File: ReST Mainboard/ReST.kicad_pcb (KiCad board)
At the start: 2 copper layers, 100 x 100 mm, 104 parts, among them IC1 AT24C128, P1 CONN_02X08, P10 CONN_01X04, P11 CONN_01X04, P12 CONN_02X04, P13 CONN_01X03, P14 CONN_02X03, P15 CONN_01X05, P16 CONN_01X03, P17 CONN_01X04, P18 CONN_02X04, P19 CONN_01X04, P2 CONN_02X08, P20 CONN_02X04, P21 CONN_02X04, P22 CONN_01X03, P23 SCREW_01X03, P24 CONN_01X03, P25 SCREW_01X03, P26 CONN_01X03, P27 SCREW_01X03, P28 CONN_01X03, P29 SCREW_01X03, P3 CONN_02X07, P30 CONN_01X03, P31 SCREW_01X03, P32 CONN_01X03, P33 SCREW_01X03, P34 CONN_01X03, P35 SCREW_01X04, P36 SCREW_01X04, P37 SCREW_01X04, P38 SCREW_01X04, P39 CONN_02X04, P4 CONN_02X10, P40 CONN_01X04, P41 CONN_01X04, P42 CONN_01X04, P43 CONN_02X03, P44 CONN_02X03, P45 CONN_02X03, P46 CONN_02X03, P5 USB_OTG, P6 CONN_02X05, P7 CONN_02X05, P8 CONN_01X09, P9 CONN_01X02, SW1 SW-SPST-NO, U1 STM32F103VE, U2 USBLC6-2, U3 L7805ACD2T-TR, U4 LM2574N-ADJ, U5 POLOLU_A4988, U6 POLOLU_A4988, U7 POLOLU_A4988, U8 POLOLU_A4988, X1 Crystal_Small

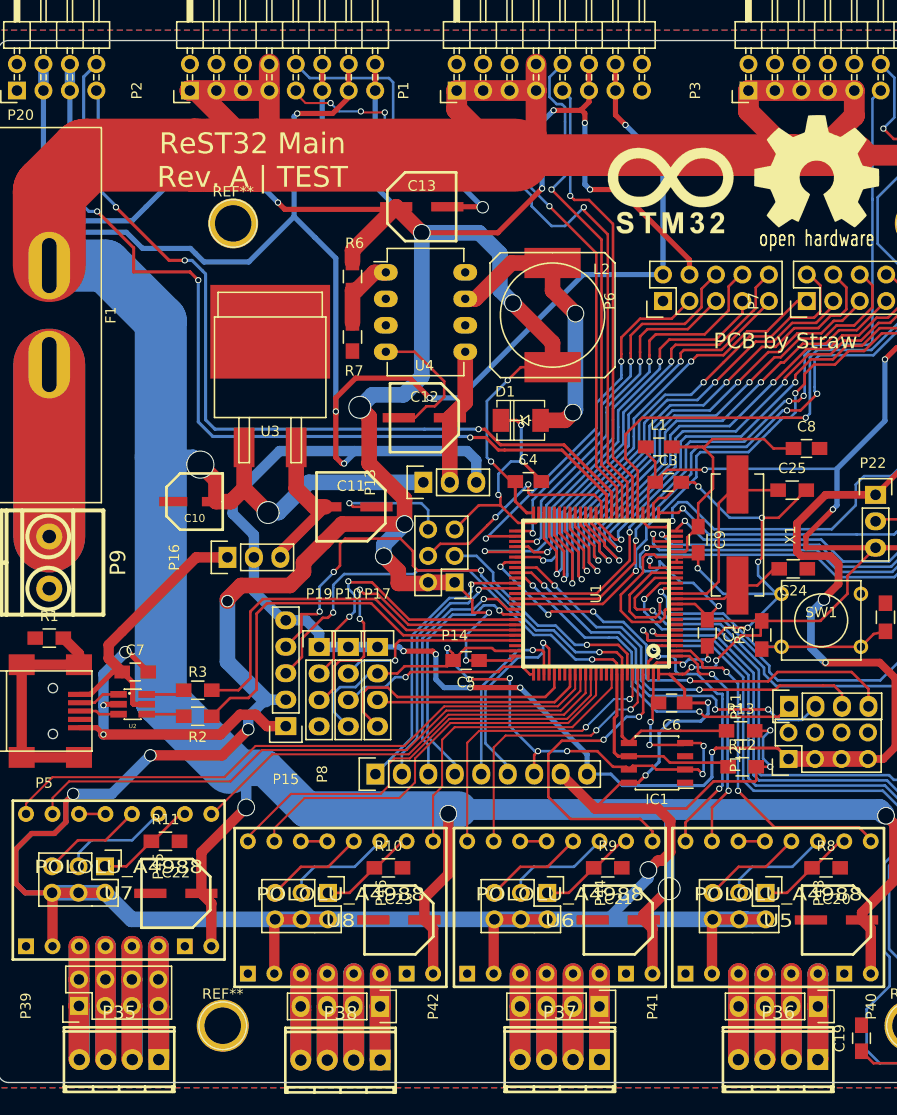
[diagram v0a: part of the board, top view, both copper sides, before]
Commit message: Finally removed all unnecessary Libs and added Heatsink for 5V Regulator
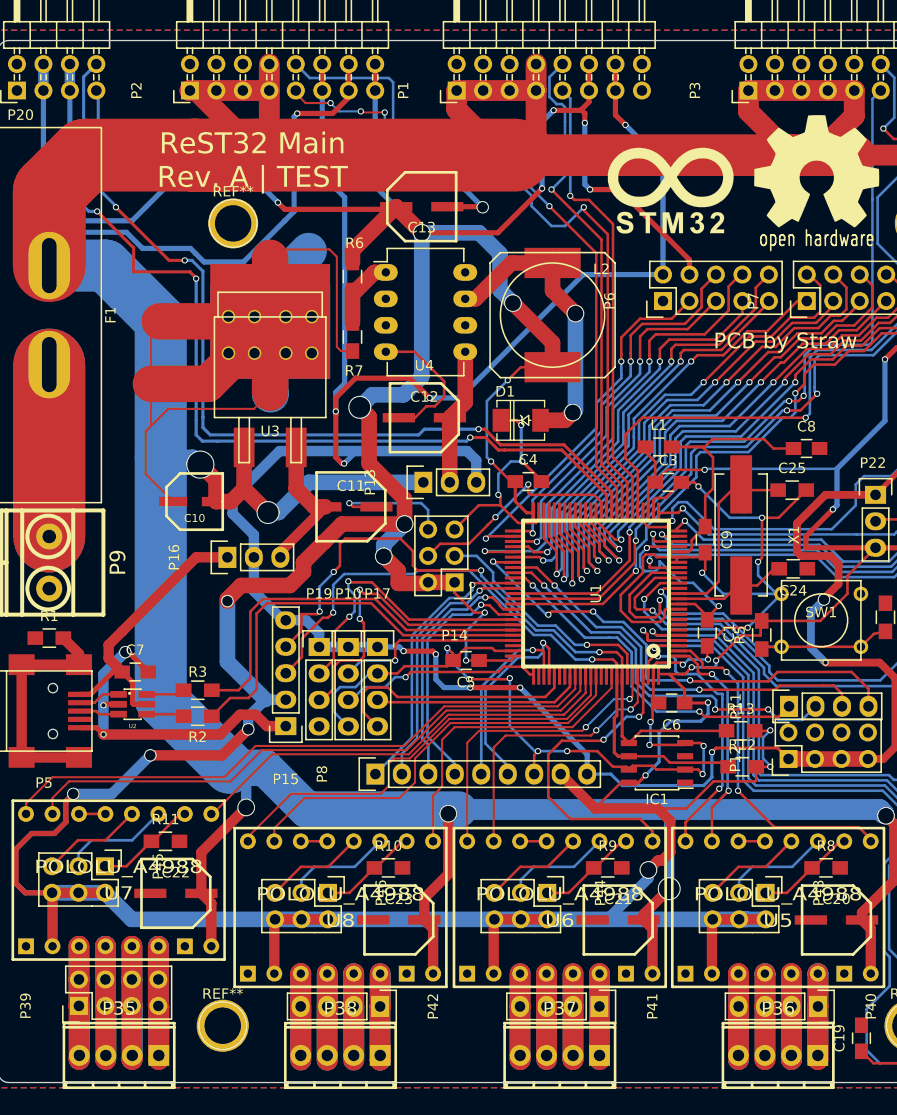
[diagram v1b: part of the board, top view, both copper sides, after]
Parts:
- C10: footprint ok-polcaps-panasonic:CP-PANASONIC-SMT_C -> ReST-Library:CP-PANASONIC-SMT_C
- C11, C12, C13: footprint ok-polcaps-panasonic:CP-PANASONIC-SMT_D -> ReST-Library:CP-PANASONIC-SMT_D
- C20, C21, C22, C23: footprint ok-polcaps-panasonic:CP-PANASONIC-SMT_D8 -> ReST-Library:CP-PANASONIC-SMT_D8
- U1: footprint ok-ic-smd:LQFP100-14x14 -> ReST-Library:LQFP100-14x14
- U3: footprint TO_SOT_Packages_SMD:SOT-404 -> ReST-Library:SOT-404
- moved C9 0.68 mm to (167.3, 103.3)
- moved P38 0.45 mm to (132.3, 152.8)
- moved P35 0.40 mm to (111.0, 152.8)
- moved P36 0.40 mm to (174.3, 152.8)
- moved P37 0.40 mm to (153.3, 152.8)
- moved X1 0.35 mm to (170.8, 102.9)
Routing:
- net GND: track 261.6 -> 364.0 mm
- net +5V: track 320.6 -> 327.7 mm
- net /SERVO1: track 46.4 -> 47.9 mm
- net /PWM-BED: track 86.8 -> 88.1 mm
- net /T0: track 81.0 -> 82.1 mm
- net Net-(C8-Pad1): track 24.2 -> 25.0 mm
- net /EXTRA2: track 24.1 -> 24.9 mm
- net +3V3: track 652.6 -> 652.0 mm

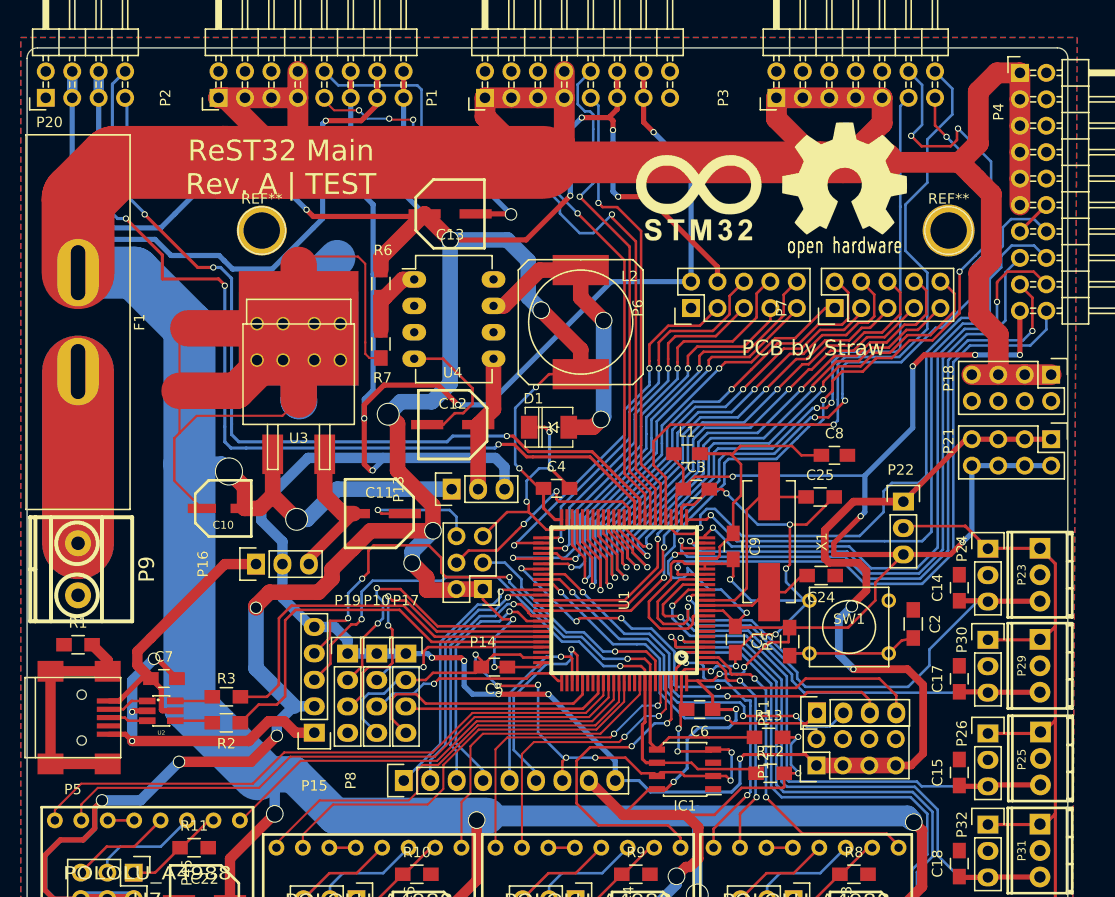
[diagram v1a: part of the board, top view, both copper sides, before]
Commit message: Added IRLML2502 Module and added Ground vias everywhere
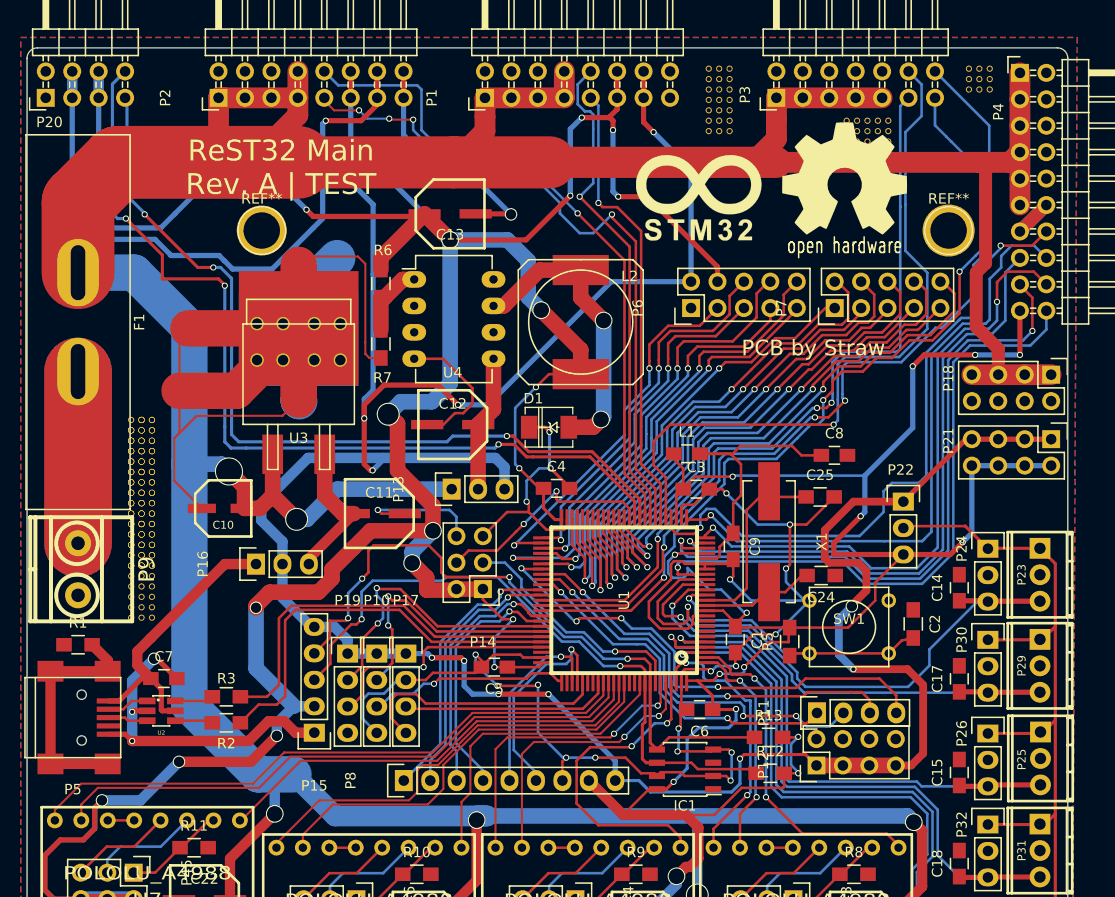
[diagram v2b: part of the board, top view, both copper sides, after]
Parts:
- added 1111: , ReST-Library:VIA-0.6mm, F.Cu at (189.9, 57.5)
- added 11111: , ReST-Library:VIA-0.6mm, F.Cu at (164.9, 57.5)
- added 111111: , ReST-Library:VIA-0.6mm, F.Cu at (178.2, 62.5)
- added 11111110, 111111110, 1111111110: , ReST-Library:VIA-0.6mm, F.Cu at (109.5, 100.2)
- added 11111111, 111111111, 1111111111: , ReST-Library:VIA-0.6mm, F.Cu at (109.5, 101.2)
- added 111111111: , ReST-Library:VIA-0.6mm, F.Cu at (109.5, 91.2)
- added 1111111112, 111111112, 11111112: , ReST-Library:VIA-0.6mm, F.Cu at (109.5, 102.2)
- added 1111111113, 111111113, 11111113: , ReST-Library:VIA-0.6mm, F.Cu at (109.5, 103.2)
- added 1111111114, 111111114, 11111114: , ReST-Library:VIA-0.6mm, F.Cu at (109.5, 104.2)
- added 1111111115, 111111115, 11111115: , ReST-Library:VIA-0.6mm, F.Cu at (109.5, 105.2)
- added 1111111116: , ReST-Library:VIA-0.6mm, F.Cu at (109.5, 106.2)
- added 1111111117: , ReST-Library:VIA-0.6mm, F.Cu at (109.5, 107.2)
- added 1111111118: , ReST-Library:VIA-0.6mm, F.Cu at (109.5, 108.2)
- added 1111111119: , ReST-Library:VIA-0.6mm, F.Cu at (109.5, 109.2)
- added 111111112, 11111112, 1111112: , ReST-Library:VIA-0.6mm, F.Cu at (109.5, 92.2)
- added 1111111120: , ReST-Library:VIA-0.6mm, F.Cu at (109.5, 110.2)
- added 111111113, 11111113, 1111113: , ReST-Library:VIA-0.6mm, F.Cu at (109.5, 93.2)
- added 111111114, 11111114, 1111114: , ReST-Library:VIA-0.6mm, F.Cu at (109.5, 94.2)
- added 111111115, 11111115, 1111115: , ReST-Library:VIA-0.6mm, F.Cu at (109.5, 95.2)
- added 111111116, 11111116, 1111116: , ReST-Library:VIA-0.6mm, F.Cu at (109.5, 96.2)
- added 111111117, 11111117, 1111117: , ReST-Library:VIA-0.6mm, F.Cu at (109.5, 97.2)
- added 111111118, 11111118, 1111118: , ReST-Library:VIA-0.6mm, F.Cu at (109.5, 98.2)
- added 111111119, 11111119, 1111119: , ReST-Library:VIA-0.6mm, F.Cu at (109.5, 99.2)
- added 111111121, 11111121, 1111121: , ReST-Library:VIA-0.6mm, F.Cu at (110.5, 91.2)
- added 1111111210, 111111210, 11111210: , ReST-Library:VIA-0.6mm, F.Cu at (110.5, 100.2)
- added 1111111211, 111111211, 11111211: , ReST-Library:VIA-0.6mm, F.Cu at (110.5, 101.2)
- added 1111111212, 111111212, 11111212: , ReST-Library:VIA-0.6mm, F.Cu at (110.5, 102.2)
- added 1111111213, 111111213, 11111213: , ReST-Library:VIA-0.6mm, F.Cu at (110.5, 103.2)
- added 1111111214, 111111214, 11111214: , ReST-Library:VIA-0.6mm, F.Cu at (110.5, 104.2)
- added 1111111215, 111111215, 11111215: , ReST-Library:VIA-0.6mm, F.Cu at (110.5, 105.2)
- added 1111111216: , ReST-Library:VIA-0.6mm, F.Cu at (110.5, 106.2)
- added 1111111217: , ReST-Library:VIA-0.6mm, F.Cu at (110.5, 107.2)
- added 1111111218: , ReST-Library:VIA-0.6mm, F.Cu at (110.5, 108.2)
- added 1111111219: , ReST-Library:VIA-0.6mm, F.Cu at (110.5, 109.2)
- added 111111122, 11111122, 1111122: , ReST-Library:VIA-0.6mm, F.Cu at (110.5, 92.2)
- added 1111111220: , ReST-Library:VIA-0.6mm, F.Cu at (110.5, 110.2)
- added 111111123, 11111123, 1111123: , ReST-Library:VIA-0.6mm, F.Cu at (110.5, 93.2)
- added 111111124, 11111124, 1111124: , ReST-Library:VIA-0.6mm, F.Cu at (110.5, 94.2)
- added 111111125, 11111125, 1111125: , ReST-Library:VIA-0.6mm, F.Cu at (110.5, 95.2)
- added 111111126, 11111126, 1111126: , ReST-Library:VIA-0.6mm, F.Cu at (110.5, 96.2)
- added 111111127, 11111127, 1111127: , ReST-Library:VIA-0.6mm, F.Cu at (110.5, 97.2)
- added 111111128, 11111128, 1111128: , ReST-Library:VIA-0.6mm, F.Cu at (110.5, 98.2)
- added 111111129, 11111129, 1111129: , ReST-Library:VIA-0.6mm, F.Cu at (110.5, 99.2)
- added 111111131, 11111131: , ReST-Library:VIA-0.6mm, F.Cu at (111.5, 91.2)
- added 1111111310, 111111310: , ReST-Library:VIA-0.6mm, F.Cu at (111.5, 100.2)
- added 1111111311, 111111311: , ReST-Library:VIA-0.6mm, F.Cu at (111.5, 101.2)
- added 1111111312, 111111312: , ReST-Library:VIA-0.6mm, F.Cu at (111.5, 102.2)
- added 1111111313, 111111313: , ReST-Library:VIA-0.6mm, F.Cu at (111.5, 103.2)
- added 1111111314, 111111314: , ReST-Library:VIA-0.6mm, F.Cu at (111.5, 104.2)
- added 1111111315, 111111315: , ReST-Library:VIA-0.6mm, F.Cu at (111.5, 105.2)
- added 1111111316: , ReST-Library:VIA-0.6mm, F.Cu at (111.5, 106.2)
- added 1111111317: , ReST-Library:VIA-0.6mm, F.Cu at (111.5, 107.2)
- added 1111111318: , ReST-Library:VIA-0.6mm, F.Cu at (111.5, 108.2)
- added 1111111319: , ReST-Library:VIA-0.6mm, F.Cu at (111.5, 109.2)
- added 111111132, 11111132: , ReST-Library:VIA-0.6mm, F.Cu at (111.5, 92.2)
- added 1111111320: , ReST-Library:VIA-0.6mm, F.Cu at (111.5, 110.2)
- added 111111133, 11111133: , ReST-Library:VIA-0.6mm, F.Cu at (111.5, 93.2)
- added 111111134, 11111134: , ReST-Library:VIA-0.6mm, F.Cu at (111.5, 94.2)
- added 111111135, 11111135: , ReST-Library:VIA-0.6mm, F.Cu at (111.5, 95.2)
- added 111111136, 11111136: , ReST-Library:VIA-0.6mm, F.Cu at (111.5, 96.2)
- added 111111137, 11111137: , ReST-Library:VIA-0.6mm, F.Cu at (111.5, 97.2)
- added 111111138, 11111138: , ReST-Library:VIA-0.6mm, F.Cu at (111.5, 98.2)
- added 111111139, 11111139: , ReST-Library:VIA-0.6mm, F.Cu at (111.5, 99.2)
- added 111112: , ReST-Library:VIA-0.6mm, F.Cu at (178.2, 63.5)
- added 111113: , ReST-Library:VIA-0.6mm, F.Cu at (178.2, 64.5)
- added 11112: , ReST-Library:VIA-0.6mm, F.Cu at (164.9, 58.5)
- added 111121: , ReST-Library:VIA-0.6mm, F.Cu at (179.2, 62.5)
- added 111122: , ReST-Library:VIA-0.6mm, F.Cu at (179.2, 63.5)
- added 111123: , ReST-Library:VIA-0.6mm, F.Cu at (179.2, 64.5)
- added 11113: , ReST-Library:VIA-0.6mm, F.Cu at (164.9, 59.5)
- added 111131: , ReST-Library:VIA-0.6mm, F.Cu at (180.2, 62.5)
- added 111132: , ReST-Library:VIA-0.6mm, F.Cu at (180.2, 63.5)
- added 111133: , ReST-Library:VIA-0.6mm, F.Cu at (180.2, 64.5)
- added 11114: , ReST-Library:VIA-0.6mm, F.Cu at (164.9, 60.5)
- added 111141: , ReST-Library:VIA-0.6mm, F.Cu at (181.2, 62.5)
- added 111142: , ReST-Library:VIA-0.6mm, F.Cu at (181.2, 63.5)
- added 111143: , ReST-Library:VIA-0.6mm, F.Cu at (181.2, 64.5)
- added 11115: , ReST-Library:VIA-0.6mm, F.Cu at (164.9, 61.5)
- added 111151: , ReST-Library:VIA-0.6mm, F.Cu at (182.2, 62.5)
- added 111152: , ReST-Library:VIA-0.6mm, F.Cu at (182.2, 63.5)
- added 111153: , ReST-Library:VIA-0.6mm, F.Cu at (182.2, 64.5)
- added 11116: , ReST-Library:VIA-0.6mm, F.Cu at (164.9, 62.5)
- added 11117: , ReST-Library:VIA-0.6mm, F.Cu at (164.9, 63.5)
- added 1112: , ReST-Library:VIA-0.6mm, F.Cu at (189.9, 58.5)
- added 11121: , ReST-Library:VIA-0.6mm, F.Cu at (165.9, 57.5)
- added 11122: , ReST-Library:VIA-0.6mm, F.Cu at (165.9, 58.5)
- added 11123: , ReST-Library:VIA-0.6mm, F.Cu at (165.9, 59.5)
- added 11124: , ReST-Library:VIA-0.6mm, F.Cu at (165.9, 60.5)
- added 11125: , ReST-Library:VIA-0.6mm, F.Cu at (165.9, 61.5)
- added 11126: , ReST-Library:VIA-0.6mm, F.Cu at (165.9, 62.5)
- added 11127: , ReST-Library:VIA-0.6mm, F.Cu at (165.9, 63.5)
- added 1113: , ReST-Library:VIA-0.6mm, F.Cu at (189.9, 59.5)
- added 11131: , ReST-Library:VIA-0.6mm, F.Cu at (166.9, 57.5)
- added 11132: , ReST-Library:VIA-0.6mm, F.Cu at (166.9, 58.5)
- added 11133: , ReST-Library:VIA-0.6mm, F.Cu at (166.9, 59.5)
- added 11134: , ReST-Library:VIA-0.6mm, F.Cu at (166.9, 60.5)
- added 11135: , ReST-Library:VIA-0.6mm, F.Cu at (166.9, 61.5)
- added 11136: , ReST-Library:VIA-0.6mm, F.Cu at (166.9, 62.5)
- added 11137: , ReST-Library:VIA-0.6mm, F.Cu at (166.9, 63.5)
- added 1121: , ReST-Library:VIA-0.6mm, F.Cu at (190.9, 57.5)
- added 1122: , ReST-Library:VIA-0.6mm, F.Cu at (190.9, 58.5)
- added 1123: , ReST-Library:VIA-0.6mm, F.Cu at (190.9, 59.5)
- added 1131: , ReST-Library:VIA-0.6mm, F.Cu at (191.9, 57.5)
- added 1132: , ReST-Library:VIA-0.6mm, F.Cu at (191.9, 58.5)
- added 1133: , ReST-Library:VIA-0.6mm, F.Cu at (191.9, 59.5)
- added ?: 1pin, ReST-Library:1pin, F.Cu at (189.9, 57.7)
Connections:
- P3 pad 12: /PWM-ADD2 -> /PWM-ADD0
- P3 pad 14: /PWM-ADD0 -> /PWM-ADD2
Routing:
- net +12V: track 473.4 -> 436.1 mm
- net /PWM-ADD2: track 90.4 -> 83.3 mm, vias 5 -> 3
- net GND: track 364.0 -> 367.6 mm
- net /E2-EN: track 64.7 -> 62.8 mm, vias 1 -> 2
- net /PWM-ADD0: track 70.3 -> 68.9 mm
- net /PWM-ADD1: vias 4 -> 3

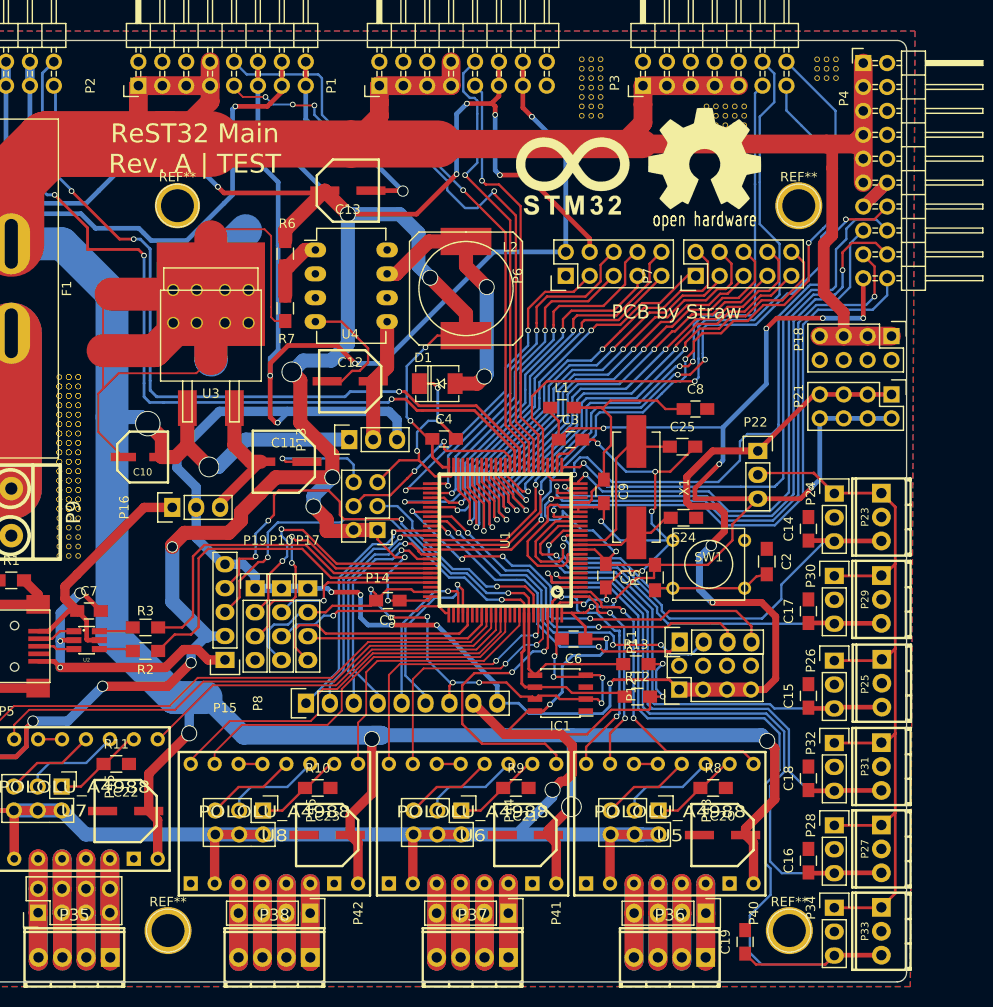
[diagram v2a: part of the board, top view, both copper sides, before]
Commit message: Added BOM for all Items + suggested Links
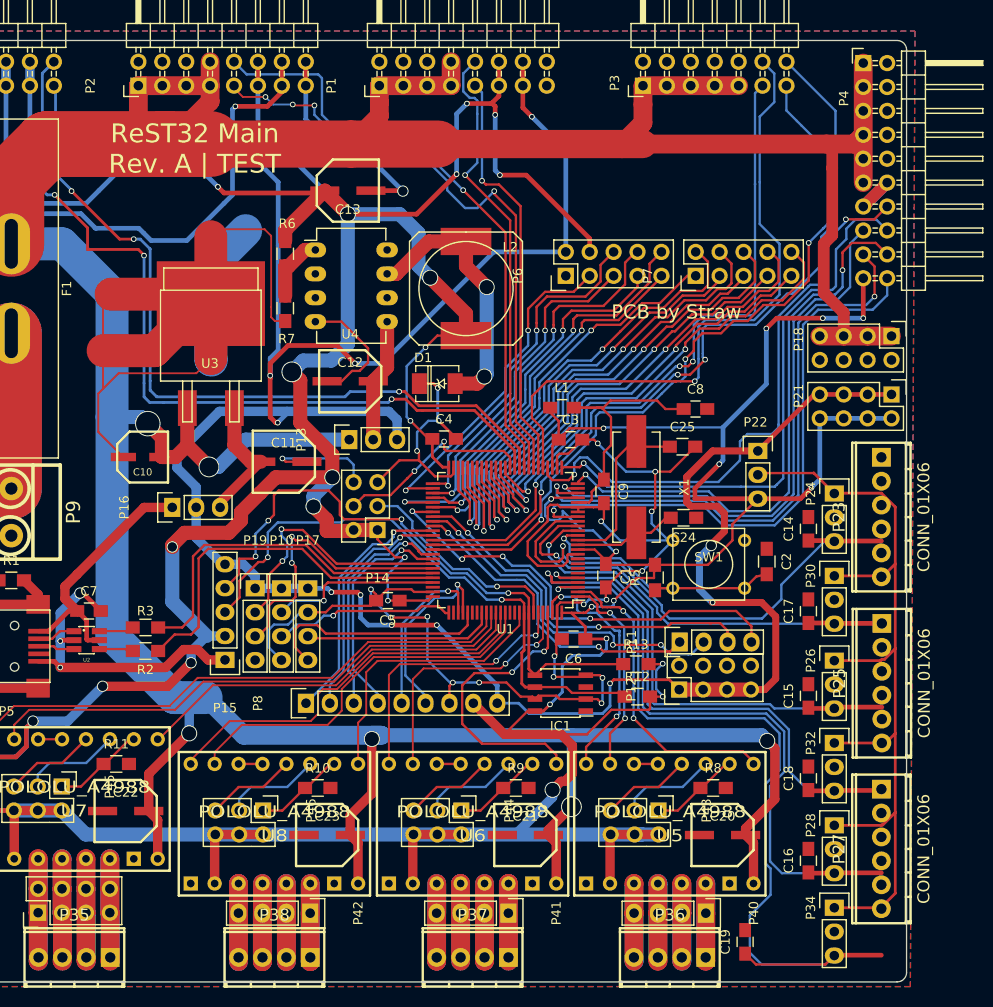
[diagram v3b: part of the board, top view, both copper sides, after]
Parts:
- removed 1111, 11111, 111111, 11111110, 11111111, 111111110, 111111111 (x2), 1111111110, 1111111111, 1111111112, 1111111113, 1111111114, 1111111115, 1111111116, 1111111117, 1111111118, 1111111119, 111111112 (x2), 1111111120, 111111113 (x2), 111111114 (x2), 111111115 (x2), 111111116, 111111117, 111111118, 111111119, 11111112 (x2), 111111121, 1111111210, 1111111211, 1111111212, 1111111213, 1111111214, 1111111215, 1111111216, 1111111217, 1111111218, 1111111219, 111111122, 1111111220, 111111123, 111111124, 111111125, 111111126, 111111127, 111111128, 111111129, 11111113 (x2), 111111131, 1111111310, 1111111311, 1111111312, 1111111313, 1111111314, 1111111315, 1111111316, 1111111317, 1111111318, 1111111319, 111111132, 1111111320, 111111133, 111111134, 111111135, 111111136, 111111137, 111111138, 111111139, 11111114 (x2), 11111115 (x2), 11111116, 11111117, 11111118, 11111119, 1111112, 11111121, 111111210, 111111211, 111111212, 111111213, 111111214, 111111215, 11111122, 11111123, 11111124, 11111125, 11111126, 11111127, 11111128, 11111129, 1111113, 11111131, 111111310, 111111311, 111111312, 111111313, 111111314, 111111315, 11111132, 11111133, 11111134, 11111135, 11111136, 11111137, 11111138, 11111139, 1111114, 1111115, 1111116, 1111117, 1111118, 1111119, 111112, 1111121, 11111210, 11111211, 11111212, 11111213, 11111214, 11111215, 1111122, 1111123, 1111124, 1111125, 1111126, 1111127, 1111128, 1111129, 111113, 11112, 111121, 111122, 111123, 11113, 111131, 111132, 111133, 11114, 111141, 111142, 111143, 11115, 111151, 111152, 111153, 11116, 11117, 1112, 11121, 11122, 11123, 11124, 11125, 11126, 11127, 1113, 11131, 11132, 11133, 11134, 11135, 11136, 11137, 1121, 1122, 1123, 1131, 1132, 1133: , ReST-Library:VIA-0.6mm
- removed ?: 1pin, ReST-Library:1pin
- removed G***: LOGO, ReST-Library:Logo_silk_OSHW_12x13mm
- removed G***: LOGO, ReST-Library:STM32-12mm
- removed P29, P31, P33: SCREW_01X03, 2:mpt_0,5%2f3-2,54
- removed REF** (x4): 1pin, Connect:1pin
- P23, P25, P27: value SCREW_01X03 -> CONN_01X06; footprint 2:mpt_0,5%2f3-2,54 -> 2:mpt_0,5%2f6-2,54
- U1: footprint ReST-Library:LQFP100-14x14 -> Housings_QFP:TQFP-100_14x14mm_Pitch0.5mm
- U3: footprint ReST-Library:SOT-404 -> TO_SOT_Packages_SMD:SOT-404
- turned U1 to 180 degrees
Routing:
- net /ENDSTOP_VCC: track 92.3 -> 38.9 mm
- net /X-MAX: track 48.2 -> 78.5 mm
- net /Y-MAX: track 57.7 -> 78.7 mm
- net (no net): track 0.00 -> 15.3 mm
- net GND: track 367.6 -> 352.3 mm
- net /Z-MAX: track 88.6 -> 90.8 mm
